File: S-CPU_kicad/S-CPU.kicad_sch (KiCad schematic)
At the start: 385 parts, among them U6 IAOO1, U8 IAOO0

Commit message: Bit DMA section update. Untangled a lot of singals. DMA addressing decoding worked out + connections to DMA RAM.
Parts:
- gave numbers to parts that had none: 3
- renumbered MCCZ1 to PKFR
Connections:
- net DMA_OFF: no longer OMNN.1
- net ~{DMA_RD}: now also OMVB.3
- net wNBBM_wNAQE_XIN/2: now reaches NAQE.2, NBBM.2
- net wOBXZ_wOCHV_XIN/2: now reaches OBXZ.2, OCHV.2
- net wNBKW_wNBPG_XIN/4: now reaches NBKW.2, NBPG.2
- net wOAFI_wOACU_XIN/4: now reaches OACU.2, OAFI.2
- net ~{DMA_WR}: now reaches PKFR.3
- new net DMA_CLK: OMNN.1
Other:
- note added: "JBNA = JBQK set to '1' when in MODE2-3, in MODE7, in MODE1 + RDY = 0 or DMA is OFF"
- note removed: "JBNA = JBQK set to '1' when in MODE2-3, in MODE7, in MODE1 + RDY = 0 or DMA is on?"
- note removed: "TCLK o DMA section"

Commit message: NOR SR latch identified.
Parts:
- removed DBWG, DBZJ: OR_4, symbol Ricoh_Cells:OR_4
- removed DCBP, DMA?: OR_2, symbol Ricoh_Cells:OR_2
- removed EBSG, EBVQ, EBXE, EBYP, ECCU, ECEK, ECGN, ECGO: DFFR_A, symbol Ricoh_Cells:DFFR_A
- removed OBEE, PAWC: AND_2, symbol Ricoh_Cells:AND_2
- removed OKHF: INVERTER_A, symbol Ricoh_Cells:INVERTER_A
- removed UBNH: NAND_5, symbol Ricoh_Cells:NAND_5
- added PAWC: NOR_LATCH, symbol Ricoh_Cells:NOR_LATCH
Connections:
- net at PBEG.6 (Q): now also PAWC.1 (SET)
- net at PAWH.3: now also PAWC.4 (RESET)
- net H146_OR_H150: no longer names the net of PASU.1
- net H146_OR_H150: now also PAWC.3 (Q)
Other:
- moved on the sheet: MAMK, OAHW, OALA, ODYH, PASU, PAWH, PBAD, PBEG, QBOC, ~{DRAMMODE}

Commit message: DMA logic update + some mistakes found in gate identification. Found while working out the DMA priority encoder.
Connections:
- net wNBEG_wNBEB_XIN/8: now reaches NBEB.2, NBEG.2, OAOU.3 (CLK), OAOU.4 (~{CLK})
- net RISING_HBLANK: now reaches OBEQ.3
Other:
- sheet OTHER_42XX_REGISTERS ports: added RISING_VBLANK; removed none
- note removed: "To DMA too"
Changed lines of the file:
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@@
     (effects (font (size 1.27 1.27)) (justify left bottom))
   )
-  (text "To DMA" (at 436.245 767.715 0)
-    (effects (font (size 1.27 1.27)) (justify left bottom))
-  )
   (text "To DMA section" (at 392.43 702.31 0)
     (effects (font (size 1.27 1.27)) (justify left bottom))
@@
     (effects (font (size 1.27 1.27)) (justify left bottom))
   )
-  (text "To DMA too" (at 300.99 709.295 0)
-    (effects (font (size 1.27 1.27)) (justify left bottom))
-  )
   (text "To DMA" (at 436.245 732.79 0)
     (effects (font (size 1.27 1.27)) (justify left bottom))
@@
     (effects (font (size 1.27 1.27)) (justify left))
   )
+  (hierarchical_label "wNBEG_wNBEB_XIN{slash}8" (shape output) (at 311.785 709.295 0) (fields_autoplaced)
+    (effects (font (size 1.27 1.27)) (justify left))
+  )
+  (hierarchical_label "RISING_HBLANK" (shape output) (at 440.69 767.715 0) (fields_autoplaced)
+    (effects (font (size 1.27 1.27)) (justify left))
+  )
   (hierarchical_label "FALLING_VBLANK" (shape input) (at 356.235 723.265 180) (fields_autoplaced)
     (effects (font (size 1.27 1.27)) (justify right))
@@
       (effects (font (size 1.27 1.27)) (justify right))
     )
-    (pin "FALLING_VBLANK" output (at 1098.55 128.905 0)
+    (pin "FALLING_VBLANK" output (at 1098.55 141.605 0)
       (effects (font (size 1.27 1.27)) (justify right))
     )
@@
       (effects (font (size 1.27 1.27)) (justify right))
     )
+    (pin "RISING_VBLANK" output (at 1098.55 144.145 0)
+      (effects (font (size 1.27 1.27)) (justify right))
+    )

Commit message: Further updates in the DMA region. SYS clock identified at last!
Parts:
- added OMRS: INVERTER_A, symbol Ricoh_Cells:INVERTER_A
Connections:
- net DMA_CLK is gone; now on net DMA_OFF: OMNN.1
- net FromDMA: now also OMRS.1; no longer OCLX.2 (D)
- net XIN: no longer CAKS.1 (~{RESET}), CAKS.5 (~{RESET}), CAKW.1 (~{RESET}), CAKW.5 (~{RESET}), CANH.1 (~{RESET}), CANH.5 (~{RESET}), CAQL.1 (~{RESET}), CAQL.5 (~{RESET}), CBDC.1 (~{RESET}), CBDC.5 (~{RESET}), CBEP.1 (~{RESET}), CBEP.5 (~{RESET}), CBFI.1 (~{RESET}), CBFI.5 (~{RESET}), CBGC.1 (~{RESET}), CBGC.5 (~{RESET}), DBJW.1, HASI.1, IAUO.6 (Q), IAYI.2 (D)
- net wNBRL_wNBQA_XIN/4: no longer NBQA.2, NBRL.2
- net ~{XIN/8}: now reaches MAOG.3 (CLK), MAOG.4 (~{CLK}), MBDX.1, MBFM.6 (~{Q})
- net wMAGR_wMAGV: now reaches MAGR.2, MAGV.2, NBIV.3 (CLK), NBIV.4 (~{CLK}), NBIZ.3 (CLK), NBIZ.4 (~{CLK}), OBHN.3 (CLK), OBHN.4 (~{CLK}), OBIW.3 (CLK), OBIW.4 (~{CLK})
- net ~{XIN/4}: now reaches MBFM.3 (CLK), MBFM.4 (~{CLK}), MBLO.3 (CLK), MBLO.4 (~{CLK}), NBJW.2, NBQA.1, NBRL.1, NBSM.6 (~{Q})
- net XIN/2: now reaches NBCF.2, NBHJ.1, NBHM.1, NBWF.7 (Q)
- net wNAGK_wNAJD: now reaches NAGK.2, NAJD.2
- net wOCRQ_wOCRS_~{XIN/8}: now reaches OCRQ.2, OCRS.2
- net XIN/4: now reaches NAPZ.2, NBSM.7 (Q), OAFM.1, OAGC.1
- net ~{XIN/2}: now reaches NBSM.3 (CLK), NBSM.4 (~{CLK}), NBUB.2, NBWF.6 (~{Q})
- net DMA_FALLING_VBLANK: now reaches NBIE.3
- net RISING_HBLANK renamed DMA_RISING_HBLANK
- net wMBFM renamed XIN/8
- net wNBHM renamed wNBHJ_wNBHM_XIN/2
- net wNBKW_wNBPG_XIN/4 renamed wNBKW_wNBPG_~{XIN/4}
- net wOAFM renamed wOAFM_wOAGC_XIN/4
- net wOBXZ_wOCHV_XIN/2 renamed wOBXZ_wOCHV_~{XIN/2}
- new net: CAKS.1 (~{RESET}), CAKS.5 (~{RESET}), CAKW.1 (~{RESET}), CAKW.5 (~{RESET}), CANH.1 (~{RESET}), CANH.5 (~{RESET}), CAQL.1 (~{RESET}), CAQL.5 (~{RESET}), CBDC.1 (~{RESET}), CBDC.5 (~{RESET}), CBEP.1 (~{RESET}), CBEP.5 (~{RESET}), CBFI.1 (~{RESET}), CBFI.5 (~{RESET}), CBGC.1 (~{RESET}), CBGC.5 (~{RESET}), DBJW.1, HASI.1, IAUO.6 (Q), IAYI.2 (D)
- new net: OCLX.2 (D), OMRS.2
- new net wNBRL_wNBQA_~{XIN/4}: NBQA.2, NBRL.2
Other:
- sheet DMA ports: added A[0..23], DMA_CHAN[0..2], D[0..7], PA[0..7], wNBBM_wNAQE_XIN/2, wNBKW_wNBPG_XIN/4, wOAFI_wOACU_XIN/4, wOBXZ_wOCHV_XIN/2, ~{4300-437F}, ~{DMA_RD}, ~{DMA_WR}; removed none
- note added: "1 x XIN/8"
- note added: "1 x ~{XIN/256}"
- note added: "1 x ~{XIN/2}"
- note added: "1 x ~{XIN/8}"
- note added: "2 x XIN/2"
- note added: "2 x XIN/4"
- note added: "2 x ~{XIN/4}"
- note added: "OAGE is MUL DIV CLK"
- note added: "System clocks"
- note removed: "To DMA"
- note removed: "To DMA section"
- note removed: "XIN/2"
- note removed: "XIN/4"
- note removed: "XIN/8"
- note removed: "to DMA"
- moved on the sheet: JAWP, JAXO, KAAQ, KAEZ, MAAG, MABB, MAGI, MAGR, MAGV, MAOG, MAVB, MAXX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

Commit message: More updates in DMA section.
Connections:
- net wNBBM_wNAQE_XIN/2 renamed wNAQE_wNBBM_XIN/2
- net wNBEG_wNBEB_XIN/8 renamed wNBEB_wNBEG_XIN/8
- net wOAFI_wOACU_XIN/4 renamed wOACU_wOAFI_XIN/4
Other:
- sheet DMA ports: added wNAQE_wNBBM_XIN/2; removed wNBBM_wNAQE_XIN/2
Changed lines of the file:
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@@
     (effects (font (size 1.27 1.27)) (justify right bottom))
   )
-  (label "wNBEG_wNBEB_XIN{slash}8" (at 323.85 624.84 180) (fields_autoplaced)
+  (label "wNBEB_wNBEG_XIN{slash}8" (at 323.85 624.84 180) (fields_autoplaced)
     (effects (font (size 1.27 1.27)) (justify right bottom))
   )
@@
     (effects (font (size 1.27 1.27)) (justify left bottom))
   )
-  (label "wOAFI_wOACU_XIN{slash}4" (at 323.85 574.04 180) (fields_autoplaced)
+  (label "wOACU_wOAFI_XIN{slash}4" (at 323.85 574.04 180) (fields_autoplaced)
     (effects (font (size 1.27 1.27)) (justify right bottom))
   )
@@
     (effects (font (size 1.27 1.27)) (justify left bottom))
   )
-  (label "wNBBM_wNAQE_XIN{slash}2" (at 323.85 529.59 180) (fields_autoplaced)
+  (label "wNAQE_wNBBM_XIN{slash}2" (at 323.85 529.59 180) (fields_autoplaced)
     (effects (font (size 1.27 1.27)) (justify right bottom))
   )
@@
     (effects (font (size 1.27 1.27)) (justify left bottom))
   )
-  (label "wNBEG_wNBEB_XIN{slash}8" (at 472.44 675.64 0) (fields_autoplaced)
+  (label "wNBEB_wNBEG_XIN{slash}8" (at 472.44 675.64 0) (fields_autoplaced)
     (effects (font (size 1.27 1.27)) (justify left bottom))
   )
@@
     (effects (font (size 1.27 1.27)) (justify left))
   )
-  (hierarchical_label "wNBEG_wNBEB_XIN{slash}8" (shape output) (at 323.85 624.84 0) (fields_autoplaced)
+  (hierarchical_label "wNBEB_wNBEG_XIN{slash}8" (shape output) (at 323.85 624.84 0) (fields_autoplaced)
     (effects (font (size 1.27 1.27)) (justify left))
   )
@@
     (effects (font (size 1.27 1.27)) (justify left))
   )
-  (hierarchical_label "wOAFI_wOACU_XIN{slash}4" (shape output) (at 323.85 574.04 0) (fields_autoplaced)
+  (hierarchical_label "wOACU_wOAFI_XIN{slash}4" (shape output) (at 323.85 574.04 0) (fields_autoplaced)
     (effects (font (size 1.27 1.27)) (justify left))
   )
@@
     (effects (font (size 1.27 1.27)) (justify right))
   )
-  (hierarchical_label "wNBBM_wNAQE_XIN{slash}2" (shape output) (at 323.85 529.59 0) (fields_autoplaced)
+  (hierarchical_label "wNAQE_wNBBM_XIN{slash}2" (shape output) (at 323.85 529.59 0) (fields_autoplaced)
     (effects (font (size 1.27 1.27)) (justify left))
   )
@@
       (effects (font (size 1.27 1.27)) (justify left))
     )
-    (pin "wNBBM_wNAQE_XIN{slash}2" input (at 756.92 725.17 180)
+    (pin "wNAQE_wNBBM_XIN{slash}2" input (at 756.92 725.17 180)
       (effects (font (size 1.27 1.27)) (justify left))
     )

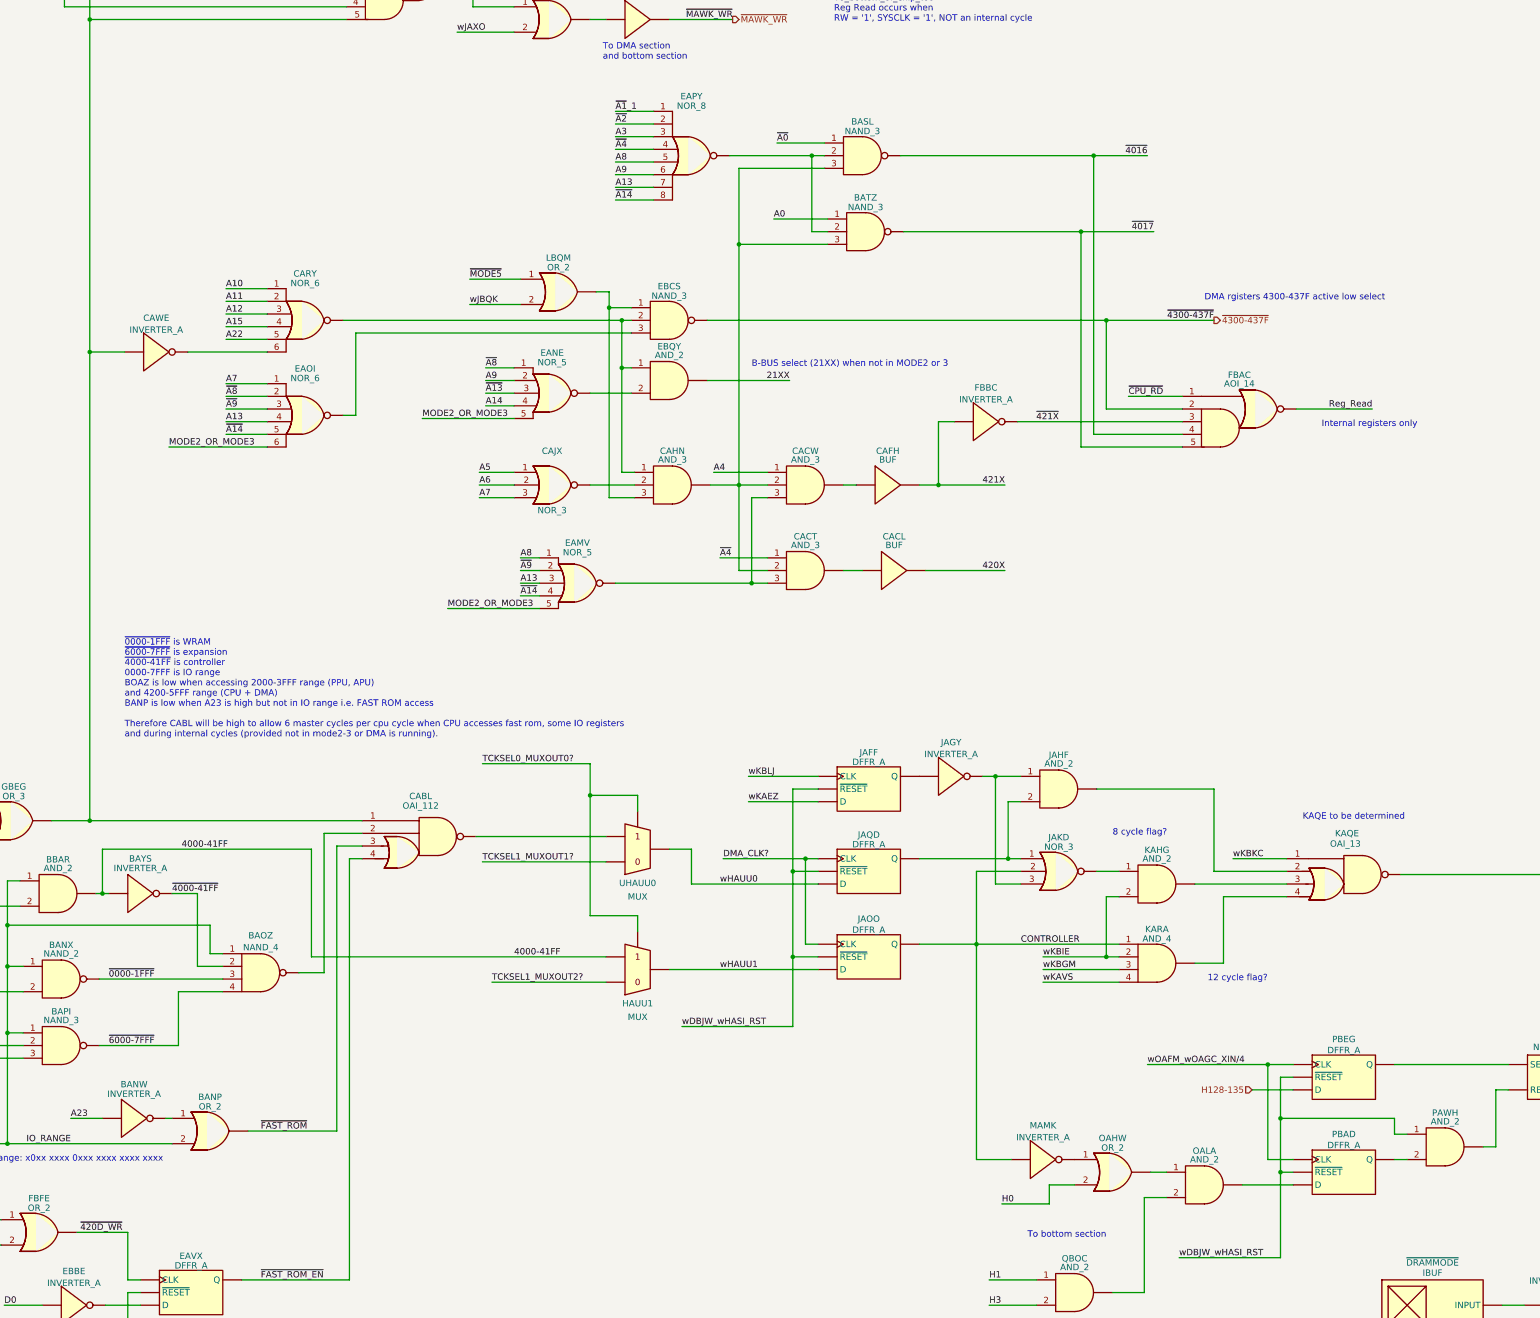
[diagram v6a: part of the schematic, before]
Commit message: Another latch with reset identified. TCKSEL demux cell worked out + notes added to schematics.
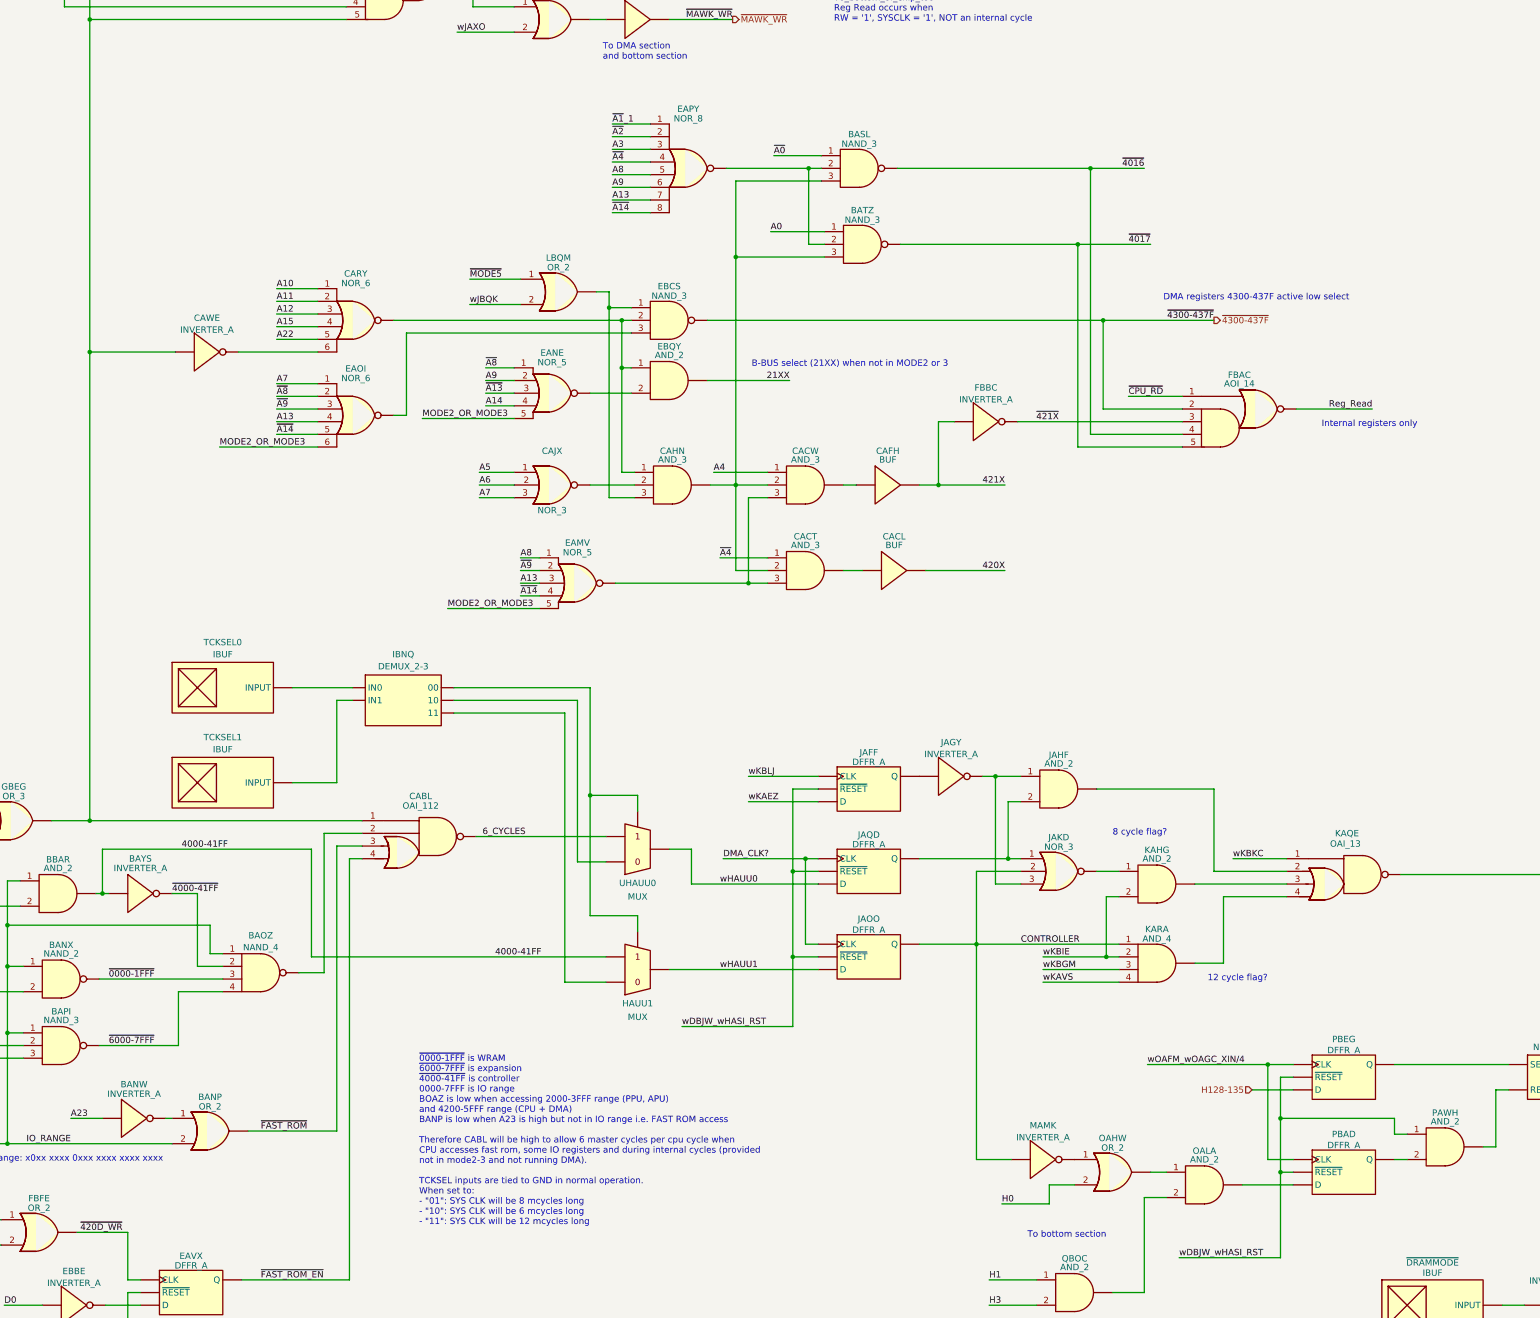
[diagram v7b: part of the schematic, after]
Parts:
- added IBNQ: DEMUX_2-3, symbol Ricoh_Cells:DEMUX_2-3
- added TCKSEL0, TCKSEL1: IBUF, symbol Ricoh_Cells:IBUF
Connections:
- net 6_CYCLES: now reaches CABL.5, UHAUU0.2
- net TCKSEL0_MUXOUT0?: no longer names the net of HAUU1.1, UHAUU0.1
- net TCKSEL0_MUXOUT0?: now also IBNQ. (IN1)
- net TCKSEL1_MUXOUT1?: no longer names the net of UHAUU0.3
- net TCKSEL1_MUXOUT1?: now also IBNQ. (IN1)
- net TCKSEL1_MUXOUT2?: no longer names the net of HAUU1.3
- net TCKSEL1_MUXOUT2?: now also IBNQ. (IN1)
- new net: IBNQ. (IN1), TCKSEL1.1 (INPUT)
- new net: IBNQ. (IN1), TCKSEL0.1 (INPUT)
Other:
- note added: "DMA registers 4300-437F active low select"
- note removed: "DMA rgisters 4300-437F active low select"
- note removed: "KAQE to be determined"
- moved on the sheet: BASL, BATZ, CARY, CAWE, EAOI, EAPY

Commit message: Almost all cells captured in schematicAlmost all cells captured in schematics. Enter the commit message for your changes. Lines starting
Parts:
- gave numbers to parts that had none: 2
- renumbered UHAUU0 to HAUU0
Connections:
- net wDBJW_wHASI_RST: now also CAKS.1 (~{RESET}), CAKS.5 (~{RESET}), CAKW.1 (~{RESET}), CAKW.5 (~{RESET}), CANH.1 (~{RESET}), CANH.5 (~{RESET}), CAQL.1 (~{RESET}), CAQL.5 (~{RESET}), CBDC.1 (~{RESET}), CBDC.5 (~{RESET}), CBEP.1 (~{RESET}), CBEP.5 (~{RESET}), CBFI.1 (~{RESET}), CBFI.5 (~{RESET}), CBGC.1 (~{RESET}), CBGC.5 (~{RESET})
- net at OMRS.2: now also OCLC.2 (D); no longer OCLX.2 (D)
- net FromDMA renamed ~{wZOOJ}
- net ~{wZOOJ}: no longer OCLC.2 (D)
- net XIN/8 renamed wMBFM_XIN/8
- net ~{XIN/8} renamed ~{wMBFM}_~{XIN/8}
- new net: DBJW.1, HASI.1, IAUO.6 (Q), IAYI.2 (D)
- new net wUOGG: OCLX.2 (D)
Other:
- note added: "RESET"
- note removed: "XIN/256"
- moved on the sheet: AAVE, AAXD, ACKS, BBFY, BBHQ, BBKM, BBKY, BBNU, BCGJ, CAKS, CAKW, CANH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
